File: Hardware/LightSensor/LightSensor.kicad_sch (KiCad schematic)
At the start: 3 parts, among them J1 Conn_01x02, Q1 KPS-3227

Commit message: Ajout fichier de production de la carte LightSensor
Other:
- company: AM163 -> antoine163
- title: BleSmartLock - LightSensor -> Ble Smart Lock - Light Sensor
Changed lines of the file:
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@@
 	(paper "A4")
 	(title_block
-		(title "BleSmartLock - LightSensor")
-		(date "2024-03-12")
+		(title "Ble Smart Lock - Light Sensor")
+		(date "2024-03-31")
 		(rev "1.0")
-		(company "AM163")
+		(company "antoine163")
 	)
 	(junction

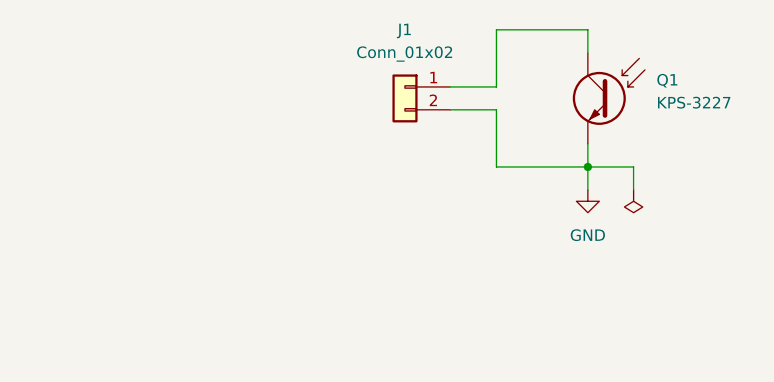
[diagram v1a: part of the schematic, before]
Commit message: Mise a jour pcb en v1.1 et readme
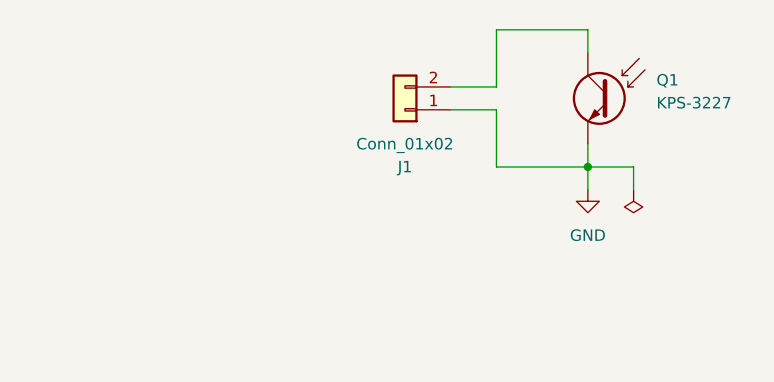
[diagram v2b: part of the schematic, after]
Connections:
- net GND: now also J1.1 (Pin_1); no longer J1.2 (Pin_2)
- net at Q1.1, Q1.3: now also J1.2 (Pin_2); no longer J1.1 (Pin_1)
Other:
- moved on the sheet: J1
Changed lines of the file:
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@@
 	(title_block
 		(title "Ble Smart Lock - Light Sensor")
-		(date "2024-03-31")
-		(rev "1.0")
+		(date "2024-05-19")
+		(rev "1.1")
 		(company "antoine163")
 	)
@@
 	(symbol
 		(lib_id "Connector_Generic:Conn_01x02")
-		(at 138.43 92.71 0)
-		(mirror y)
+		(at 138.43 95.25 180)
 		(unit 1)
 		(exclude_from_sim no)
@@
 		(dnp no)
 		(property "Reference" "J1"
-			(at 138.43 86.36 0)
+			(at 138.43 101.6 0)
 			(effects
 				(font
@@
 		)
 		(property "Value" "Conn_01x02"
-			(at 138.43 88.9 0)
+			(at 138.43 99.06 0)
 			(effects
 				(font
@@
 		)
 		(property "Footprint" "Connector_JST:JST_PH_B2B-PH-K_1x02_P2.00mm_Vertical"
-			(at 138.43 92.71 0)
+			(at 138.43 95.25 0)
 			(effects
 				(font
@@
 		)
 		(property "Datasheet" "~"
-			(at 138.43 92.71 0)
+			(at 138.43 95.25 0)
 			(effects
 				(font
@@
 		)
 		(property "Description" "Generic connector, single row, 01x02, script generated (kicad-library-utils/schlib/autogen/connector/)"
-			(at 138.43 92.71 0)
+			(at 138.43 95.25 0)
 			(effects
 				(font
@@
 		)
 		(property "Vendor" "JST:B2B-PH-K-S"
-			(at 138.43 92.71 0)
+			(at 138.43 95.25 0)
 			(effects
 				(font
